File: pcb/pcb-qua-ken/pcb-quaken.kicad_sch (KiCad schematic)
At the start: 91 parts, among them J1 Conn_01x06_MountingPin, J2 Conn_01x02_Pin, J3 Conn_01x04_Pin, SW1 SW_Push, SW2 Rotary_Encoder_Default, U1 XC6206PxxxMR, U2 STM32F401RCTx, Y1 12MHz

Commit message: schematics review with scgh
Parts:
- removed C2: 1u, Capacitor_SMD:C_0402_1005Metric, symbol Device:C_Small
- removed R2: 5.1k, Resistor_SMD:R_0402_1005Metric, symbol Device:R_Small
- C11: value 4.7 -> 100n
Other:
- note added: "??"
- moved on the sheet: C1, C14, C3, C4, C5, C6, C7

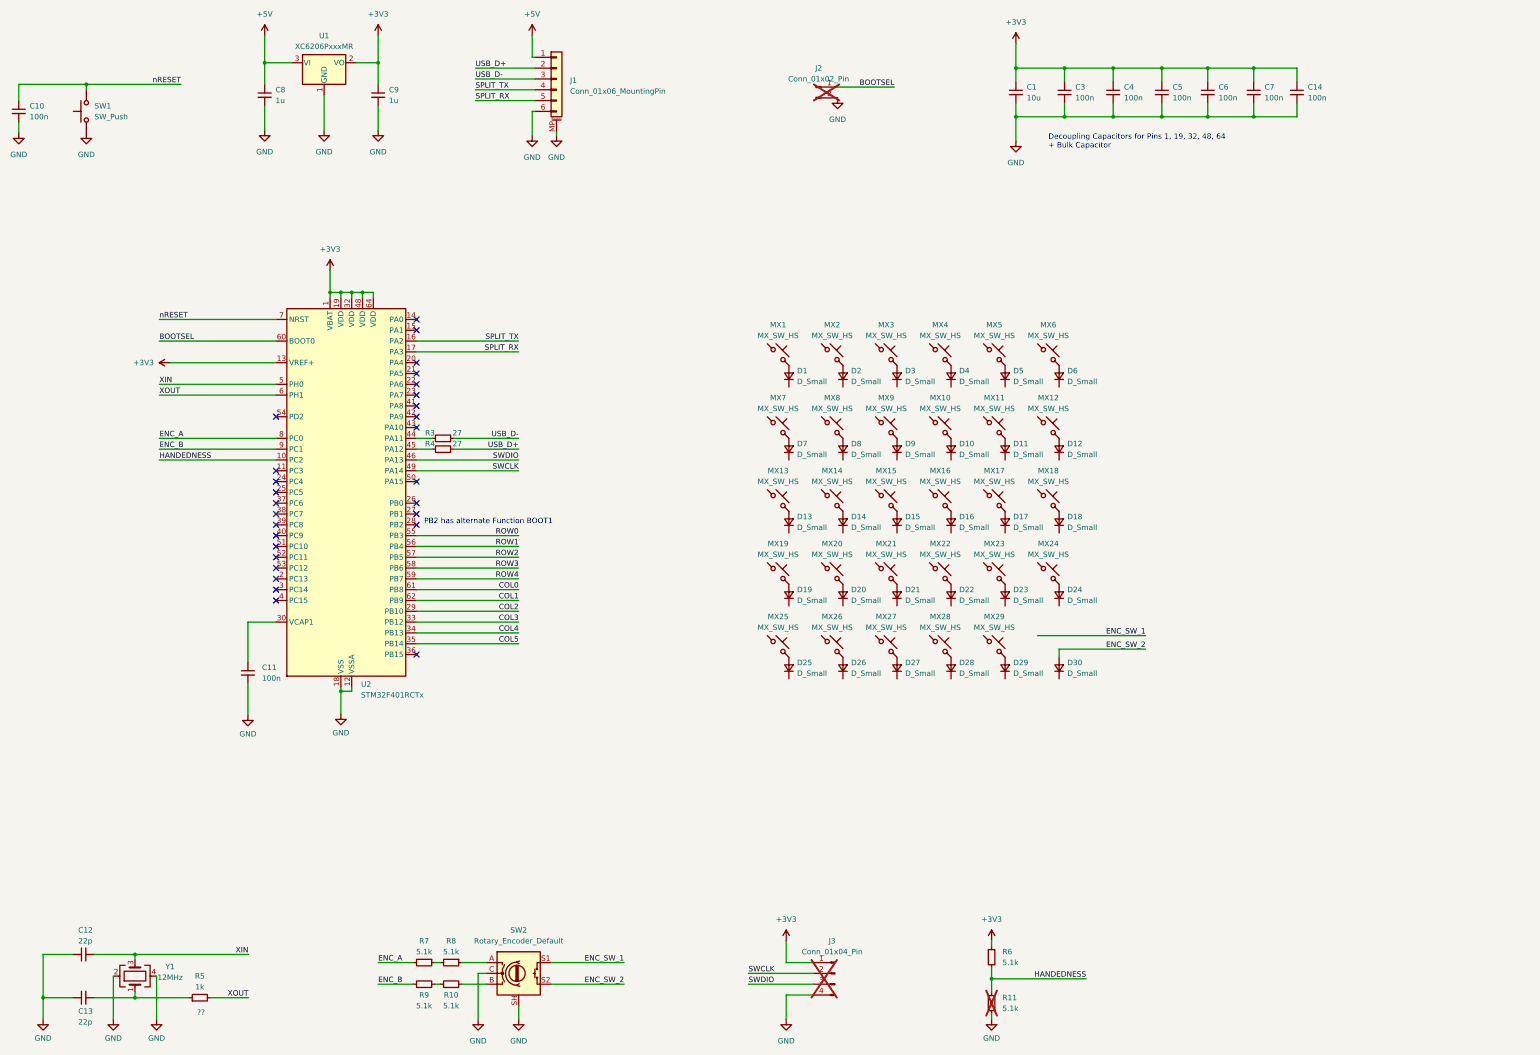
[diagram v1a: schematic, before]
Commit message: layout ready for review
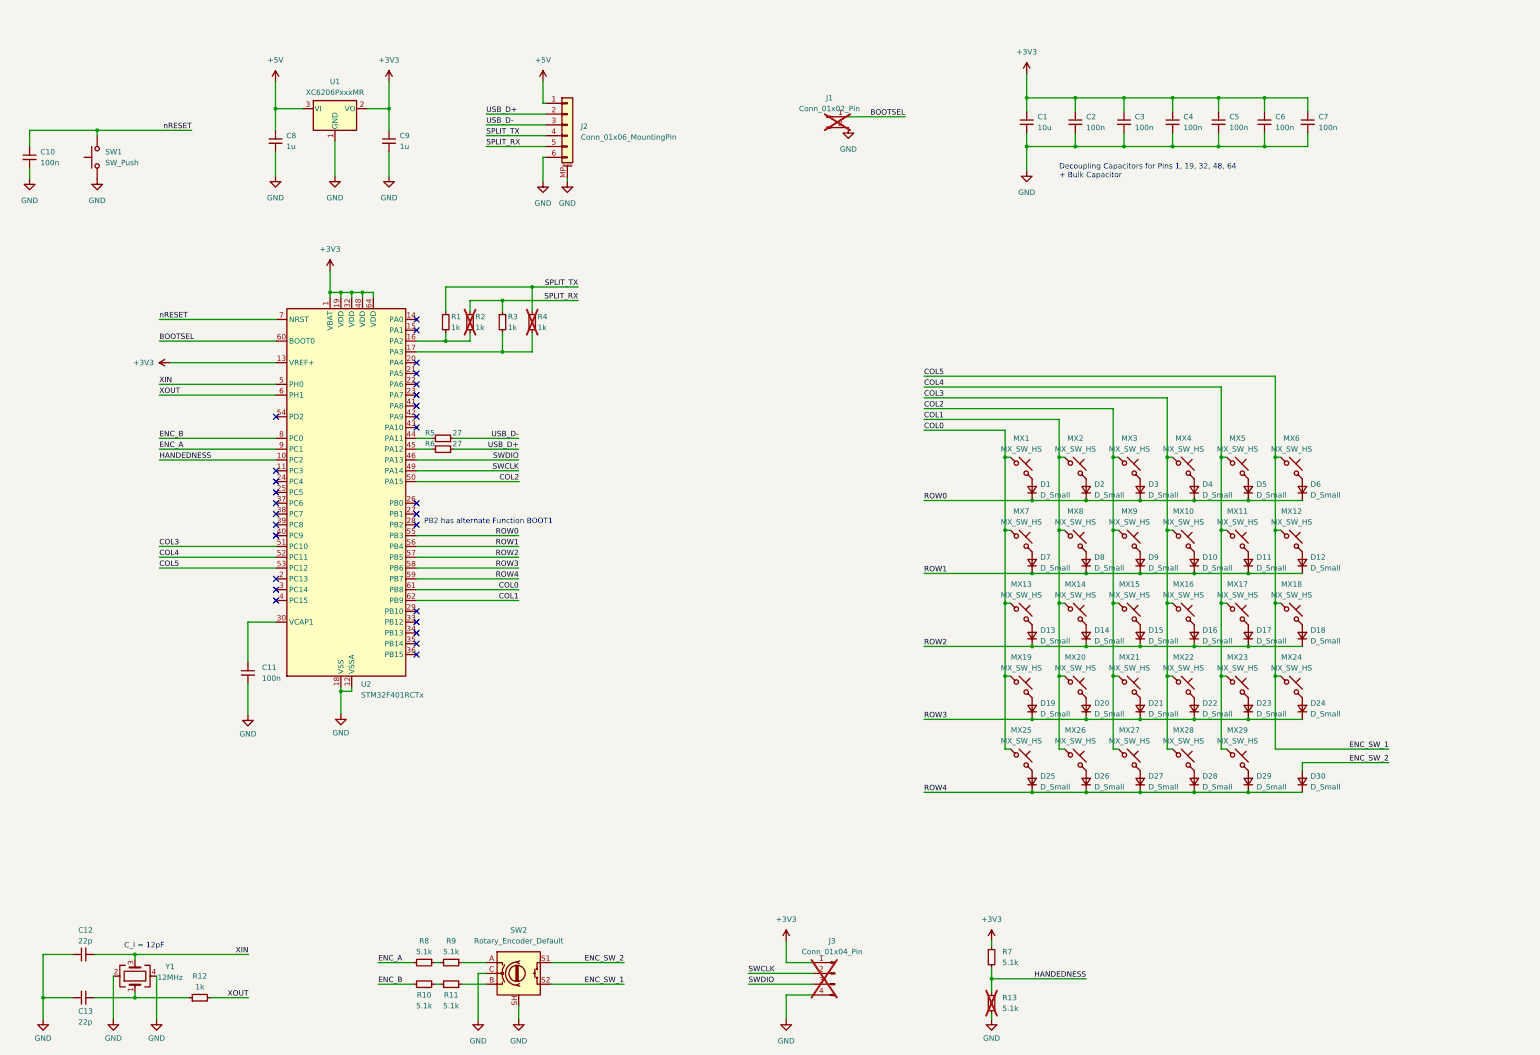
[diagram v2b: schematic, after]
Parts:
- added R1, R2, R3, R4: 1k, Resistor_SMD:R_0402_1005Metric, symbol Device:R_Small
- renumbered C3 to C2, C4 to C3, C5 to C4, C6 to C5, C7 to C6, C14 to C7, J2 to J1, J1 to J2, R9 to R10, R10 to R11, R5 to R12, R11 to R13, R3 to R5, R4 to R6, R6 to R7, R7 to R8, R8 to R9
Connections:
- net ENC_SW_1 is gone; now on net ENC_SW_2: SW2.S1
- net COL0: now also MX1.1, MX13.1, MX19.1, MX25.1, MX7.1
- net COL1: now also MX14.1, MX2.1, MX20.1, MX26.1, MX8.1
- net COL2: now also MX15.1, MX21.1, MX27.1, MX3.1, MX9.1, U2.50 (PA15); no longer U2.29 (PB10)
- net COL3: now also MX10.1, MX16.1, MX22.1, MX28.1, MX4.1, U2.51 (PC10); no longer U2.33 (PB12)
- net COL4: now also MX11.1, MX17.1, MX23.1, MX29.1, MX5.1, U2.52 (PC11); no longer U2.34 (PB13)
- net COL5: now also MX12.1, MX18.1, MX24.1, MX6.1, SW2.S2, U2.53 (PC12); no longer U2.35 (PB14)
- net ENC_A: now also U2.9 (PC1); no longer U2.8 (PC0)
- net ENC_B: now also U2.8 (PC0); no longer U2.9 (PC1)
- net ENC_SW_2: no longer SW2.S2
- net ROW0: now also D1.1 (K), D2.1 (K), D3.1 (K), D4.1 (K), D5.1 (K), D6.1 (K)
- net ROW1: now also D10.1 (K), D11.1 (K), D12.1 (K), D7.1 (K), D8.1 (K), D9.1 (K)
- net ROW2: now also D13.1 (K), D14.1 (K), D15.1 (K), D16.1 (K), D17.1 (K), D18.1 (K)
- net ROW3: now also D19.1 (K), D20.1 (K), D21.1 (K), D22.1 (K), D23.1 (K), D24.1 (K)
- net ROW4: now also D25.1 (K), D26.1 (K), D27.1 (K), D28.1 (K), D29.1 (K), D30.1 (K)
- net SPLIT_RX: now also R2.1, R3.1; no longer U2.17 (PA3)
- net SPLIT_TX: now also R1.1, R4.1; no longer U2.16 (PA2)
- new net: R3.2, R4.2, U2.17 (PA3)
- new net: R1.2, R2.2, U2.16 (PA2)
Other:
- note added: "C_l = 12pF"
- note removed: "??"
- moved on the sheet: C1, C10, C2, C3, C4, C5, C6, C7, C8, C9, D1, D10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

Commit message: removed one switch from the thumb cluster
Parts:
- removed D25: D_Small, Diode_SMD:D_SOD-123, symbol Device:D_Small
- removed MX25: MX_SW_HS, PCM_marbastlib-mx:SW_MX_HS_1u, symbol PCM_marbastlib-mx:MX_SW_HS
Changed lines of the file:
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@@
   (junction (at 323.215 49.53) (diameter 0) (color 0 0 0 0)
   )
-  (junction (at 268.605 201.295) (diameter 0) (color 0 0 0 0)
-  )
   (junction (at 278.765 49.53) (diameter 0) (color 0 0 0 0)
   )
@@
   )
   (junction (at 267.335 49.53) (diameter 0) (color 0 0 0 0)
-  )
-  (junction (at 262.255 173.99) (diameter 0) (color 0 0 0 0)
   )
   (junction (at 290.195 49.53) (diameter 0) (color 0 0 0 0)
@@
     (stroke (width 0) (type default))
   )
-  (wire (pts (xy 262.255 191.135) (xy 263.525 191.135))
-    (stroke (width 0) (type default))
-  )
   (wire (pts (xy 313.055 173.99) (xy 313.055 191.135))
     (stroke (width 0) (type default))
@@
     (stroke (width 0) (type default))
   )
-  (wire (pts (xy 268.605 201.295) (xy 281.305 201.295))
+  (wire (pts (xy 243.205 201.295) (xy 281.305 201.295))
     (stroke (width 0) (type default))
   )
@@
     (stroke (width 0) (type default))
   )
-  (wire (pts (xy 243.205 201.295) (xy 268.605 201.295))
-    (stroke (width 0) (type default))
-  )
   (wire (pts (xy 319.405 167.005) (xy 332.105 167.005))
     (stroke (width 0) (type default))
@@
   )
   (wire (pts (xy 300.355 191.135) (xy 301.625 191.135))
-    (stroke (width 0) (type default))
-  )
-  (wire (pts (xy 262.255 173.99) (xy 262.255 191.135))
     (stroke (width 0) (type default))
   )
@@
     )
   )
-  (symbol (lib_id "PCM_marbastlib-mx:MX_SW_HS") (at 266.065 193.675 0) (unit 1)
-    (in_bom yes) (on_board yes) (dnp no) (fields_autoplaced)
-    (property "Reference" "MX25" (at 266.065 186.69 0)
-      (effects (font (size 1.27 1.27)))
-    )
-    (property "Value" "MX_SW_HS" (at 266.065 189.23 0)
-      (effects (font (size 1.27 1.27)))
-    )
-    (property "Footprint" "PCM_marbastlib-mx:SW_MX_HS_1u" (at 266.065 193.675 0)
-      (effects (font (size 1.27 1.27)) hide)
-    )
-    (property "Datasheet" "~" (at 266.065 193.675 0)
-      (effects (font (size 1.27 1.27)) hide)
-    )
-    (pin "1")
-    (pin "2")
-    (instances
-      (project "pcb-quaken"
-        (path "/0fec5bf3-2c1b-43dd-91bc-92c7302749bc"
-          (reference "MX25") (unit 1)
-        )
-      )
-    )
-  )
   (symbol (lib_id "PCM_marbastlib-mx:MX_SW_HS") (at 329.565 176.53 0) (unit 1)
     (in_bom yes) (on_board yes) (dnp no) (fields_autoplaced)
@@
         )
       )
-    )
-  )
-  (symbol (lib_id "Device:D_Small") (at 268.605 198.755 90) (unit 1)
-    (in_bom yes) (on_board yes) (dnp no) (fields_autoplaced)
-    (property "Reference" "D25" (at 270.51 197.485 90)
-      (effects (font (size 1.27 1.27)) (justify right))
-    )
-    (property "Value" "D_Small" (at 270.51 200.025 90)
-      (effects (font (size 1.27 1.27)) (justify right))
-    )
-    (property "Footprint" "Diode_SMD:D_SOD-123" (at 268.605 198.755 90)
-      (effects (font (size 1.27 1.27)) hide)
-    )
-    (property "Datasheet" "~" (at 268.605 198.755 90)
-      (effects (font (size 1.27 1.27)) hide)
-    )
-    (property "Sim.Device" "D" (at 268.605 198.755 0)
-      (effects (font (size 1.27 1.27)) hide)
-    )
-    (property "Sim.Pins" "1=K 2=A" (at 268.605 198.755 0)
-      (effects (font (size 1.27 1.27)) hide)
-    )
-    (pin "2")
-    (pin "1")
-    (instances
-      (project "pcb-quaken"
-        (path "/0fec5bf3-2c1b-43dd-91bc-92c7302749bc"
-          (reference "D25") (unit 1)
-        )
-      )
